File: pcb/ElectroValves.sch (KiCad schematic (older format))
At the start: 51 parts, among them J10 Conn_01x04_Female, J11 Conn_01x04_Female, J12 Conn_01x04_Female, J3 Conn_Load, J4 Conn_Load, J5 Conn_Load, J6 Conn_Load, J7 Conn_01x04_Female, J8 Conn_01x04_Female, J9 Conn_01x04_Female, Q1 PN2222, Q2 PN2222, Q3 PN2222, Q4 PN2222, U11 AQH3213AX, U12 AQH3213AX, U13 AQH3213AX, U14 AQH3213AX, U15 PCAL6416A, U3 TLP240D, U4 TLP240D, U5 TLP240D, U6 TLP240D, U7 TLP240D, U8 TLP240D

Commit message: Connections in the schema were modified and components some components from supply and electrovalves were positioned on the PCB
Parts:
- U15: footprint Package_DFN_QFN:QFN-20-1EP_4x4mm_P0.5mm_EP2.5x2.5mm -> Package_DFN_QFN:QFN-24-1EP_4x4mm_P0.5mm_EP2.6x2.6mm
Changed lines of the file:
@@
 F 0 "U15" H 1900 5350 50  0000 C CNB
 F 1 "PCAL6416A" H 2300 3950 50  0000 C CNB
-F 2 "Package_DFN_QFN:QFN-20-1EP_4x4mm_P0.5mm_EP2.5x2.5mm" H 3300 4450 50  0001 C CNN
+F 2 "Package_DFN_QFN:QFN-24-1EP_4x4mm_P0.5mm_EP2.6x2.6mm" H 3300 4450 50  0001 C CNN
 F 3 "https://www.nxp.com/docs/en/data-sheet/PCAL6416A.pdf" H 3300 4450 50  0001 C CNN
 F 4 "568-9946-1-ND" H 2300 4200 50  0001 C CNN "DigiKey"

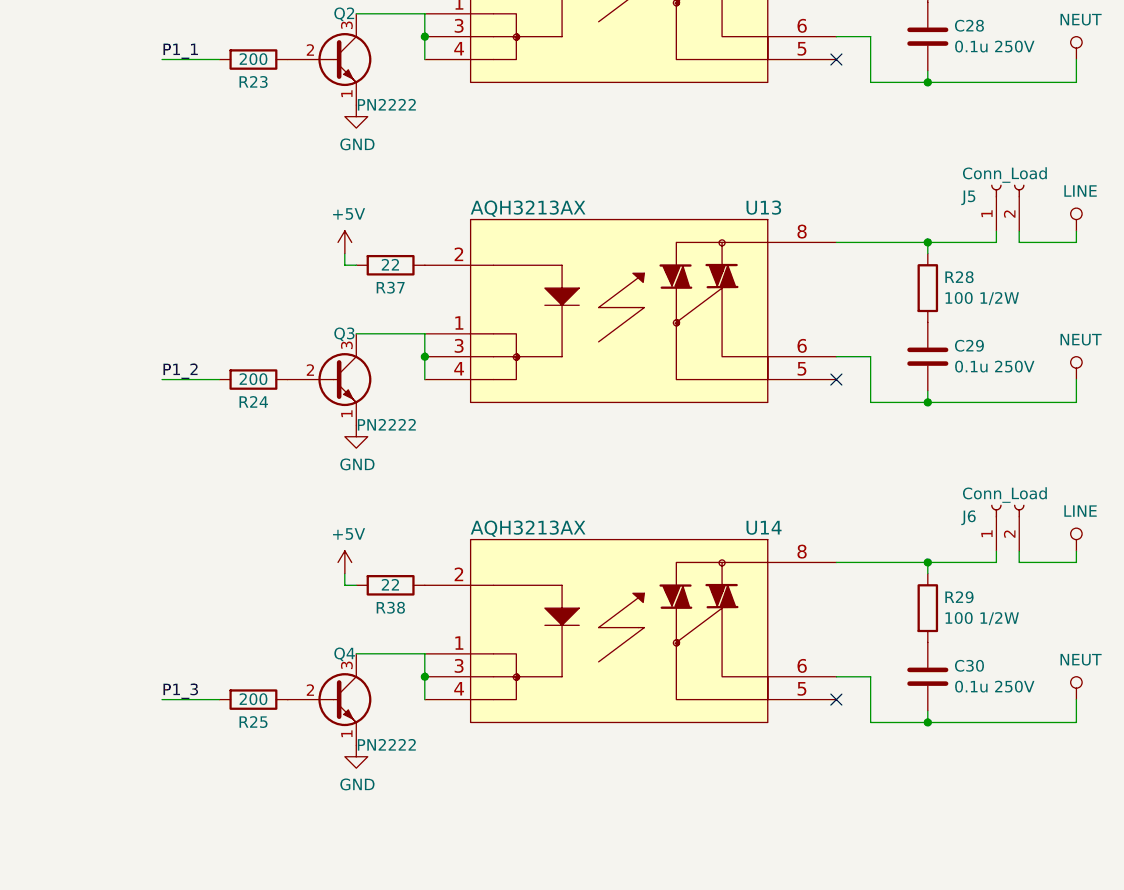
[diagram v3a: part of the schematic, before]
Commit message: STM32 added
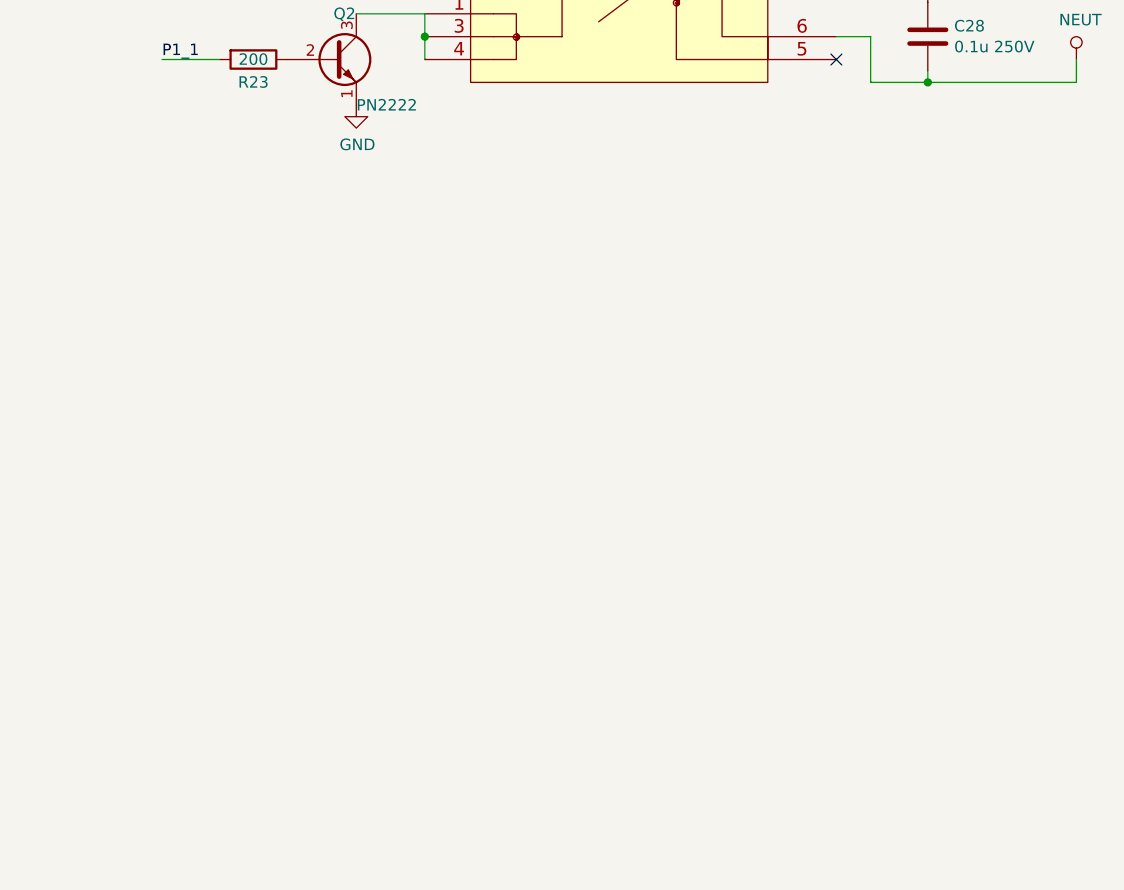
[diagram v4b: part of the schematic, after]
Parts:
- removed C29, C30: 0.1u 250V, Capacitor_SMD:C_1210_3225Metric, symbol Device:C
- removed J5, J6: Conn_Load, symbol BarrelConnector:Conn_01x02_Female
- removed Q3, Q4: PN2222, SMD:SOT23_Transistor, symbol Transistor_BJT:PN2222A
- removed R24, R25: 200, Resistor_SMD:R_0402_1005Metric, symbol Device:R
- removed R28, R29: 100 1/2W, Resistor_SMD:R_0612_1632Metric, symbol Device:R
- removed R37, R38: 22, Resistor_SMD:R_0402_1005Metric, symbol Device:R
- removed U13, U14: AQH3213AX, SMD:AQH3223A, symbol AQH3213AX:AQH3213AX
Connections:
- no-connect marks 4 -> 2

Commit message: replacement
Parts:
- removed R31, R32, R33, R34: 10k, Resistor_SMD:R_0402_1005Metric, symbol Device:R
- removed U15: PCAL6416A, Package_DFN_QFN:QFN-24-1EP_4x4mm_P0.5mm_EP2.6x2.6mm, symbol PCAL6416AHF:PCAL6416A
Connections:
- net P1_0 is gone; now on net R6: R22.2
- net P1_1 is gone; now on net R7: R23.2
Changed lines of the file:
@@
 	0    1    1    0
-$EndComp
-$Comp
-L PCAL6416AHF:PCAL6416A U15
-U 1 1 5E92BB67
-P 2300 4200
-F 0 "U15" H 1900 5350 50  0000 C CNB
-F 1 "PCAL6416A" H 2300 3950 50  0000 C CNB
-F 2 "Package_DFN_QFN:QFN-24-1EP_4x4mm_P0.5mm_EP2.6x2.6mm" H 3300 4450 50  0001 C CNN
-F 3 "https://www.nxp.com/docs/en/data-sheet/PCAL6416A.pdf" H 3300 4450 50  0001 C CNN
-F 4 "568-9946-1-ND" H 2300 4200 50  0001 C CNN "DigiKey"
-	1    2300 4200
-	1    0    0    -1
 $EndComp
 Text Label 4000 1650 0    50   ~ 0
@@
 Wire Wire Line
 	4000 3550 4100 3550
-Text Label 3150 3400 2    50   ~ 0
-R0
-Wire Wire Line
-	3150 3400 2950 3400
-Text Label 3150 3500 2    50   ~ 0
-R1
-Wire Wire Line
-	3150 3500 2950 3500
-Text Label 3150 3600 2    50   ~ 0
-R2
-Wire Wire Line
-	3150 3600 2950 3600
-Text Label 3150 3700 2    50   ~ 0
-R3
-Wire Wire Line
-	3150 3700 2950 3700
-Text Label 3150 3800 2    50   ~ 0
-R4
-Wire Wire Line
-	3150 3800 2950 3800
-Text Label 3150 3900 2    50   ~ 0
-R5
-Wire Wire Line
-	3150 3900 2950 3900
-Text HLabel 950  3850 0    50   Input ~ 0
-SCL
-Text HLabel 950  3950 0    50   BiDi ~ 0
-SDA
-Wire Wire Line
-	950  3850 1200 3850
-Wire Wire Line
-	950  3950 1350 3950
 Wire Wire Line
 	4000 6500 4100 6500
@@
 Text Label 4000 4550 0    50   ~ 0
 R3
-Text Label 3150 4000 2    50   ~ 0
+Text Label 6800 1650 0    50   ~ 0
 R6
-Wire Wire Line
-	3150 4000 2950 4000
-Text Label 3150 4100 2    50   ~ 0
+Text Label 6800 3000 0    50   ~ 0
 R7
-Wire Wire Line
-	3150 4100 2950 4100
-Wire Wire Line
-	3150 4300 2950 4300
-Wire Wire Line
-	3150 4400 2950 4400
-Wire Wire Line
-	3150 4500 2950 4500
-Wire Wire Line
-	3150 4600 2950 4600
-Wire Wire Line
-	3150 4700 2950 4700
-Wire Wire Line
-	3150 4800 2950 4800
-Wire Wire Line
-	3150 4900 2950 4900
-Wire Wire Line
-	3150 5000 2950 5000
-$Comp
-L power:GND #PWR07
-U 1 1 5E953705
-P 2300 5300
-F 0 "#PWR07" H 2300 5050 50  0001 C CNN
-F 1 "GND" H 2305 5127 50  0000 C CNN
-F 2 "" H 2300 5300 50  0001 C CNN
-F 3 "" H 2300 5300 50  0001 C CNN
-	1    2300 5300
-	1    0    0    -1
-$EndComp
-$Comp
-L ventilator-PowerSymbols:3V3_ESP #PWR08
-U 1 1 5E95424A
-P 2450 2850
-F 0 "#PWR08" H 2450 2810 30  0001 C CNN
-F 1 "3V3_ESP" H 2459 2988 30  0000 C CNN
-F 2 "" H 2450 2850 60  0000 C CNN
-F 3 "" H 2450 2850 60  0000 C CNN
-	1    2450 2850
-	1    0    0    -1
-$EndComp
-Text Label 3150 4300 2    50   ~ 0
-P1_0
-Text Label 3150 4400 2    50   ~ 0
-P1_1
-Text Label 3150 4500 2    50   ~ 0
-P1_2
-Text Label 3150 4600 2    50   ~ 0
-P1_3
-Text Label 3150 4700 2    50   ~ 0
-P1_4
-Text Label 3150 4800 2    50   ~ 0
-P1_5
-Text Label 3150 4900 2    50   ~ 0
-P1_6
-Text Label 3150 5000 2    50   ~ 0
-P1_7
-$Comp
-L power:+5V #PWR06
-U 1 1 5E95579E
-P 2200 2850
-F 0 "#PWR06" H 2200 2700 50  0001 C CNN
-F 1 "+5V" H 2215 3023 50  0000 C CNN
-F 2 "" H 2200 2850 50  0001 C CNN
-F 3 "" H 2200 2850 50  0001 C CNN
-	1    2200 2850
-	1    0    0    -1
-$EndComp
-Text Label 6800 1650 0    50   ~ 0
-P1_0
-Text Label 6800 3000 0    50   ~ 0
-P1_1
 $Comp
 L power:+5V #PWR09
@@
 	1    0    0    -1
 $EndComp
-$Comp
-L power:GND #PWR05
-U 1 1 5E9C02A4
-P 1600 3650
-F 0 "#PWR05" H 1600 3400 50  0001 C CNN
-F 1 "GND" H 1605 3477 50  0000 C CNN
-F 2 "" H 1600 3650 50  0001 C CNN
-F 3 "" H 1600 3650 50  0001 C CNN
-	1    1600 3650
-	1    0    0    -1
-$EndComp
-Wire Wire Line
-	1750 3600 1600 3600
-Wire Wire Line
-	1600 3600 1600 3650
-Text HLabel 950  3500 0    50   Input ~ 0
-RST_PCA
-Wire Wire Line
-	950  3500 1050 3500
 NoConn ~ 9750 3000
 NoConn ~ 9750 1650
-$Comp
-L Device:R R32
-U 1 1 5E9D8B5A
-P 1200 2950
-F 0 "R32" V 1250 3050 50  0000 L CNN
-F 1 "10k" V 1250 2700 50  0000 L CNN
-F 2 "Resistor_SMD:R_0402_1005Metric" V 1130 2950 50  0001 C CNN
-F 3 "~" H 1200 2950 50  0001 C CNN
-	1    1200 2950
-	1    0    0    -1
-$EndComp
-$Comp
-L Device:R R31
-U 1 1 5E9DC847
-P 1050 2950
-F 0 "R31" V 1100 3050 50  0000 L CNN
-F 1 "10k" V 1100 2700 50  0000 L CNN
-F 2 "Resistor_SMD:R_0402_1005Metric" V 980 2950 50  0001 C CNN
-F 3 "~" H 1050 2950 50  0001 C CNN
-	1    1050 2950
-	1    0    0    -1
-$EndComp
-$Comp
-L ventilator-PowerSymbols:3V3_ESP #PWR01
-U 1 1 5E9DC84D
-P 1050 2550
-F 0 "#PWR01" H 1050 2510 30  0001 C CNN
-F 1 "3V3_ESP" H 1059 2688 30  0000 C CNN
-F 2 "" H 1050 2550 60  0000 C CNN
-F 3 "" H 1050 2550 60  0000 C CNN
-	1    1050 2550
-	1    0    0    -1
-$EndComp
-$Comp
-L Device:R R34
-U 1 1 5E9E3B39
-P 1500 2950
-F 0 "R34" V 1550 3050 50  0000 L CNN
-F 1 "10k" V 1550 2700 50  0000 L CNN
-F 2 "Resistor_SMD:R_0402_1005Metric" V 1430 2950 50  0001 C CNN
-F 3 "~" H 1500 2950 50  0001 C CNN
-	1    1500 2950
-	1    0    0    -1
-$EndComp
-$Comp
-L Device:R R33
-U 1 1 5E9E3B45
-P 1350 2950
-F 0 "R33" V 1400 3050 50  0000 L CNN
-F 1 "10k" V 1400 2700 50  0000 L CNN
-F 2 "Resistor_SMD:R_0402_1005Metric" V 1280 2950 50  0001 C CNN
-F 3 "~" H 1350 2950 50  0001 C CNN
-	1    1350 2950
-	1    0    0    -1
-$EndComp
-Wire Wire Line
-	1050 3100 1050 3500
-Connection ~ 1050 3500
-Wire Wire Line
-	1050 3500 1750 3500
-Wire Wire Line
-	1200 3100 1200 3850
-Connection ~ 1200 3850
-Wire Wire Line
-	1200 3850 1750 3850
-Wire Wire Line
-	1350 3100 1350 3950
-Connection ~ 1350 3950
-Wire Wire Line
-	1350 3950 1750 3950
-Text HLabel 950  4200 0    50   Output ~ 0
-INT_PCA
-Wire Wire Line
-	950  4200 1500 4200
-Wire Wire Line
-	1500 3100 1500 4200
-Connection ~ 1500 4200
-Wire Wire Line
-	1500 4200 1750 4200
 $Comp
 L BarrelConnector:Conn_01x04_Female J7
@@
 $EndComp
 Wire Wire Line
-	1500 2650 1500 2800
-Wire Wire Line
-	1350 2650 1350 2800
-Wire Wire Line
-	1200 2800 1200 2650
-Wire Wire Line
-	1050 2650 1050 2800
-Wire Wire Line
-	2200 2850 2200 3000
-Wire Wire Line
-	2450 2850 2450 3000
-Wire Wire Line
-	1500 2650 1350 2650
-Connection ~ 1200 2650
-Wire Wire Line
-	1200 2650 1050 2650
-Connection ~ 1350 2650
-Wire Wire Line
-	1350 2650 1200 2650
-Wire Wire Line
-	1050 2550 1050 2650
-Connection ~ 1050 2650
-Wire Wire Line
 	7050 1650 6800 1650

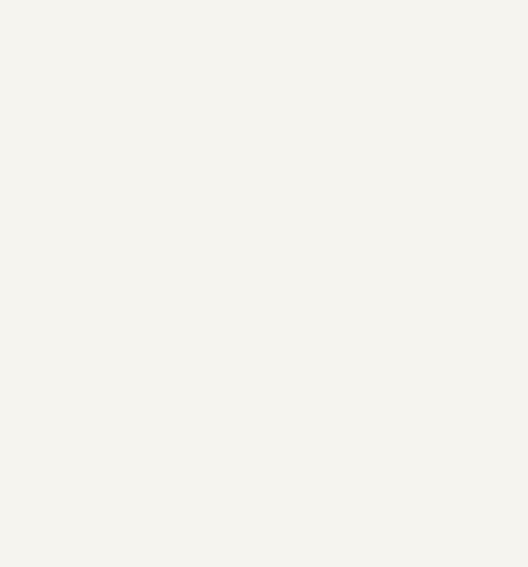
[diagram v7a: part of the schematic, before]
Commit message: connecting STM32
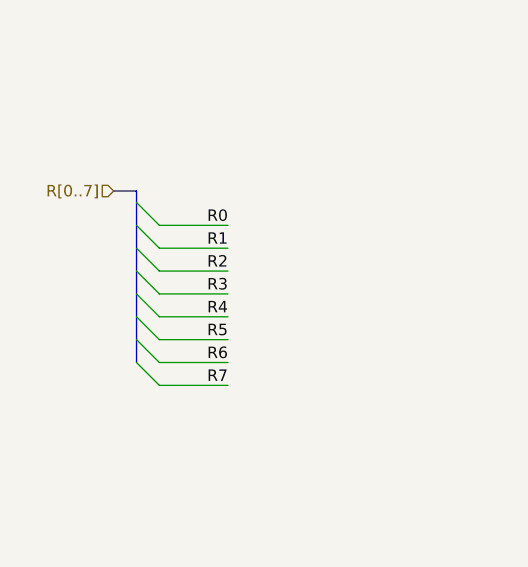
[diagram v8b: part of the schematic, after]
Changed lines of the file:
@@
 $Descr A4 11693 8268
 encoding utf-8
-Sheet 4 8
+Sheet 3 7
 Title ""
 Date ""
@@
 Wire Wire Line
 	7950 2800 7650 2800
+Wire Wire Line
+	1600 1900 1900 1900
+Text Label 1900 1900 2    50   ~ 0
+R0
+Wire Wire Line
+	1600 2000 1900 2000
+Text Label 1900 2000 2    50   ~ 0
+R1
+Wire Wire Line
+	1600 2100 1900 2100
+Text Label 1900 2100 2    50   ~ 0
+R2
+Wire Wire Line
+	1600 2200 1900 2200
+Text Label 1900 2200 2    50   ~ 0
+R3
+Wire Wire Line
+	1600 2300 1900 2300
+Text Label 1900 2300 2    50   ~ 0
+R4
+Wire Wire Line
+	1600 2400 1900 2400
+Text Label 1900 2400 2    50   ~ 0
+R5
+Wire Wire Line
+	1600 2500 1900 2500
+Text Label 1900 2500 2    50   ~ 0
+R6
+Wire Wire Line
+	1600 2600 1900 2600
+Text Label 1900 2600 2    50   ~ 0
+R7
+Entry Wire Line
+	1500 1900 1600 2000
+Entry Wire Line
+	1500 1800 1600 1900
+Entry Wire Line
+	1500 2100 1600 2200
+Entry Wire Line
+	1500 2000 1600 2100
+Entry Wire Line
+	1500 2300 1600 2400
+Entry Wire Line
+	1500 2200 1600 2300
+Entry Wire Line
+	1500 2500 1600 2600
+Entry Wire Line
+	1500 2400 1600 2500
+Wire Bus Line
+	1400 1750 1500 1750
+Wire Bus Line
+	1500 1750 1500 2500
+Text HLabel 1400 1750 0    50   Input ~ 0
+R[0..7]
 $EndSCHEMATC
